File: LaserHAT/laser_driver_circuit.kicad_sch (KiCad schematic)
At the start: 24 parts, among them Q1 Si2302CDS, Q2 Si1902DL, U1 TLV2371DBV

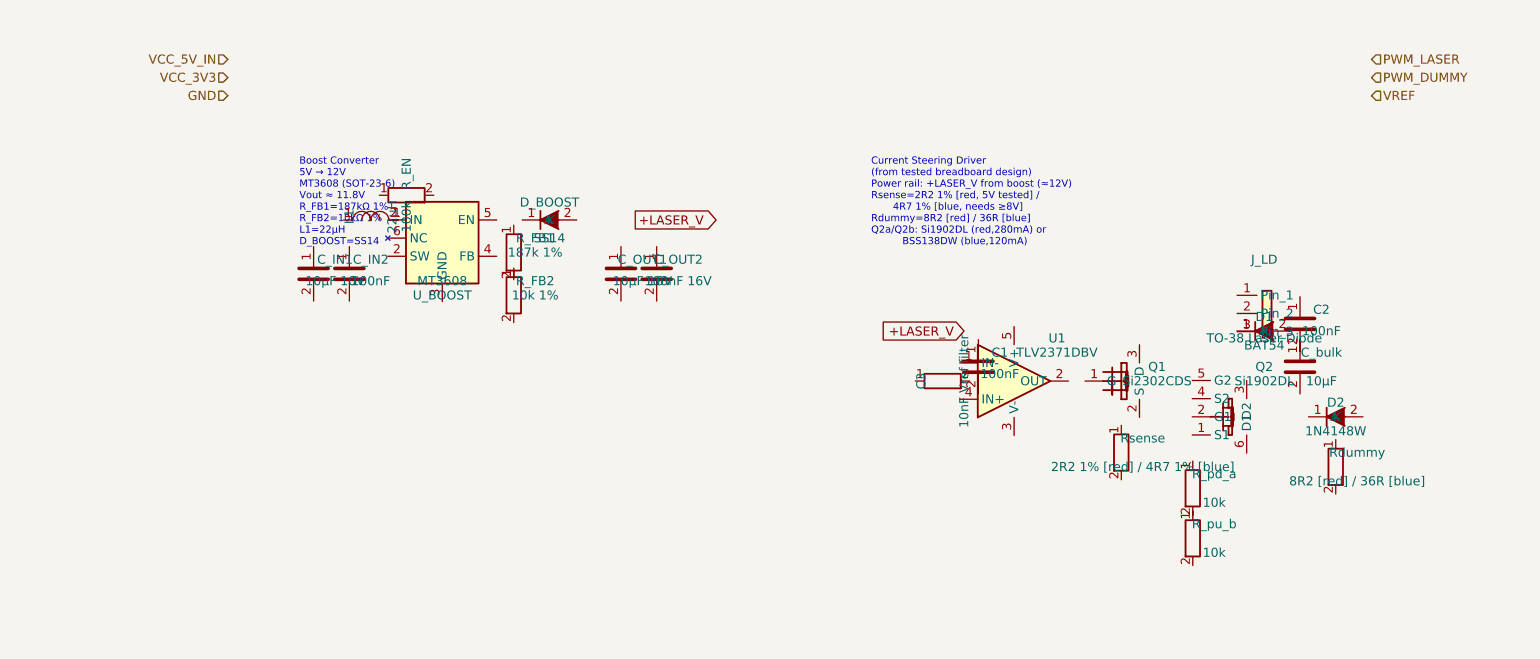
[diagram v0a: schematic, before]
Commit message: Regenerate schematics via kiutils; add generate_schematics.py
Previous hand-written schematics failed to open in eeschema due to
quoted UUIDs and unrecognised generator_version field.  Replace with
a kiutils-based Python generator that produces correctly-formatted
KiCad 9 S-expressions.

Each sheet now has:
- Unquoted UUIDs and proper PageSettings object (eeschema-compatible)
- HierarchicalLabel port declarations matching parent sheet pins
- LocalLabel net labels placed at exact pin connection points so KiCad
  can build the netlist without manual wire routing
- NoConnect markers on unused pins (SBU1/SBU2, DTR, MT3608 NC pin)
- SymbolInstance entries for BOM/netlist annotation

Add requirements.txt (kiutils==1.4.8) for reproducible environment.

Run: .venv/bin/python3 LaserHAT/generate_schematics.py

Co-Authored-By: Claude Sonnet 4.6 <noreply@anthropic.com>
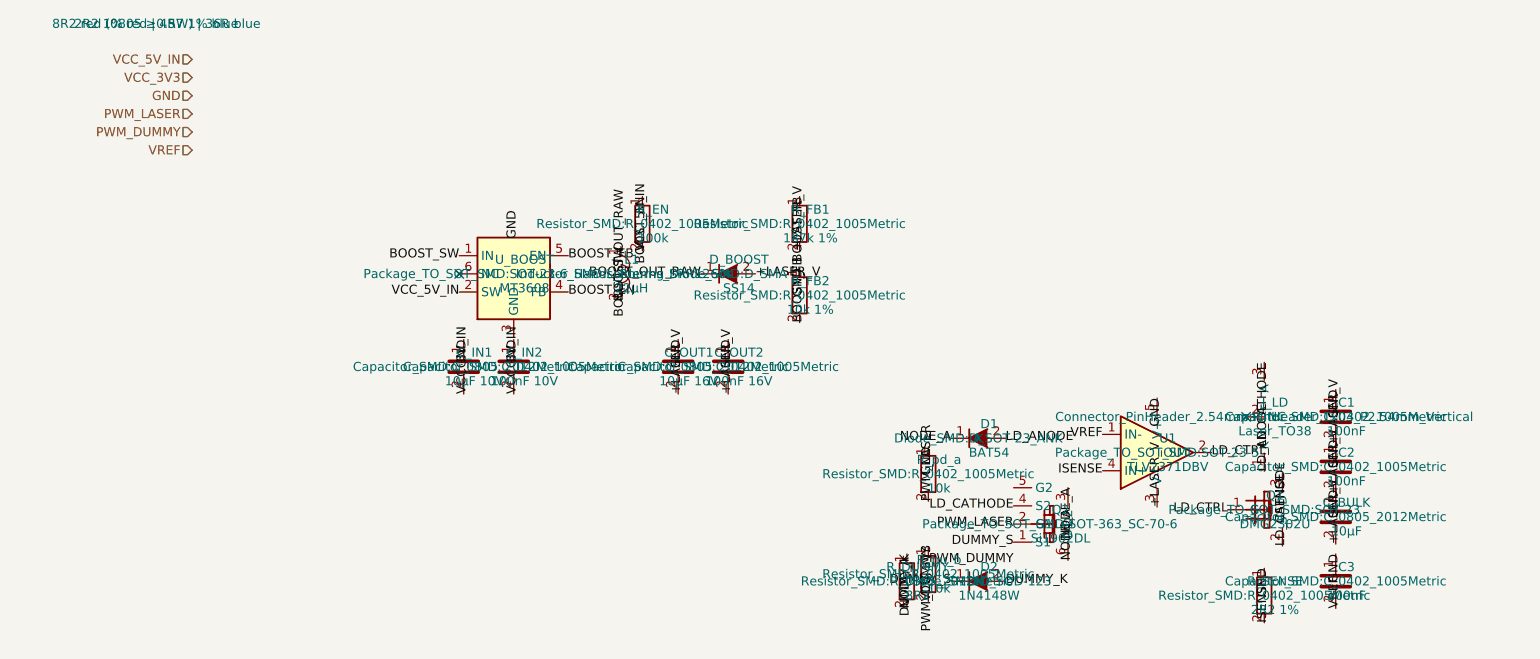
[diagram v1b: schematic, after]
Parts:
- removed C3: 10nF Vref filter, Capacitor_SMD:C_0402_1005Metric, symbol Device:R
- removed C_bulk: 10µF, Capacitor_SMD:C_0805_2012Metric, symbol Device:C
- removed J_LD: TO-38 Laser Diode, Connector_PinHeader_2.54mm:PinHeader_1x03_P2.54mm_Vertical, symbol Connector_Generic:Conn_01x03
- removed Rdummy: 8R2 [red] / 36R [blue], Resistor_SMD:R_0805_2012Metric, symbol Device:R
- removed Rsense: 2R2 1% [red] / 4R7 1% [blue], Resistor_SMD:R_0402_1005Metric, symbol Device:R
- added C3: 100nF, Capacitor_SMD:C_0402_1005Metric, symbol Device:C
- added C_BULK: 10µF, Capacitor_SMD:C_0805_2012Metric, symbol Device:C
- added J_LD: Laser_TO38, Connector_PinHeader_2.54mm:PinHeader_1x03_P2.54mm_Vertical, symbol Device:D_Laser_Photo_NType
- added R_DUMMY: 8R2, Resistor_SMD:R_0805_2012Metric, symbol Device:R
- added R_SENSE: 2R2 1%, Resistor_SMD:R_0402_1005Metric, symbol Device:R
- C_IN2: value 100nF -> 100nF 10V
- D1: footprint Diode_SMD:D_SOT-23_AnodeK1K2 -> Diode_SMD:D_SOT-23_ANK
- L1: footprint Inductor_SMD:L_4020 -> Inductor_SMD:L_Bourns_SRR1260
- Q1: value Si2302CDS -> DMG2302U
- U_BOOST: footprint Package_TO_SOT_SMD:SOT-23-6 -> Package_TO_SOT_SMD:SOT-23-6_Handsoldering
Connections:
- net +LASER_V: now also C1.2, C2.2, C_OUT1.2, C_OUT2.2, D_BOOST.2 (K), R_FB1.2, U1.3 (V-), C_BULK.2
- net GND: now also C1.1, C2.1, C_IN1.1, C_IN2.1, C_OUT1.1, C_OUT2.1, R_FB2.1, R_pd_a.1, U1.5 (V+), C3.1, C_BULK.1, R_SENSE.1
- net PWM_DUMMY: now also R_pu_b.1
- net PWM_LASER: now also Q2.2 (G1), R_pd_a.2
- net VCC_3V3: now also R_pu_b.2
- net VCC_5V_IN: now also C_IN1.2, C_IN2.2, R_EN.2, U_BOOST.2 (SW)
- net VREF: now also U1.1 (IN-), C3.2
- net BOOST_SW: now reaches U_BOOST.1 (IN)
- net BOOST_SW: now also L1.1
- net BOOST_EN: now reaches U_BOOST.4 (FB)
- net BOOST_EN: now also R_EN.1
- net BOOST_FB: now reaches U_BOOST.5 (EN)
- net BOOST_FB: now also R_FB1.1, R_FB2.2
- net BOOST_OUT_RAW: now reaches L1.2
- net BOOST_OUT_RAW: now also D_BOOST.1 (A)
- net LD_CTRL: now reaches U1.2 (OUT)
- net LD_CTRL: now also Q1.1 (G)
- net ISENSE: now reaches U1.4 (IN+)
- net ISENSE: now also Q1.3 (D), R_SENSE.2
- net LD_CATHODE: now reaches Q1.2 (S)
- net LD_CATHODE: now also Q2.4 (S2), J_LD.3 (A)
- net DUMMY_S: now reaches Q2.1 (S1)
- net DUMMY_S: now also D2.1 (A)
- net NODE_A: now reaches Q2.3 (D2)
- net NODE_A: now also D1.1 (A), Q2.6 (D1), R_DUMMY.2
- net LD_ANODE: now reaches D1.2 (K)
- net LD_ANODE: now also J_LD.1 (K)
- net DUMMY_K: now reaches D2.2 (K)
- net DUMMY_K: now also R_DUMMY.1
- no-connect marks 0 -> 2
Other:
- note removed: "Boost Converter 5V → 12V MT3608 (SOT-23-6) Vout ≈ 11.8V R_FB1=187kΩ 1% R_FB2=10kΩ 1% L1=22µH D_BOOST=SS14"
- note removed: "Current Steering Driver (from tested breadboard design) Power rail: +LASER_V from boost (≈12V) Rsense=2R2 1% [red, 5V tested] / 4R7 1% [blue, needs ≥8V] Rdummy=8R2 [red] / 36R [blue] Q2a/Q2b: Si1902DL (red,280mA) or BSS138DW (blue,120mA)"
- title: Laser Driver Circuit — Boost + Current Steering -> Laser Driver Circuit

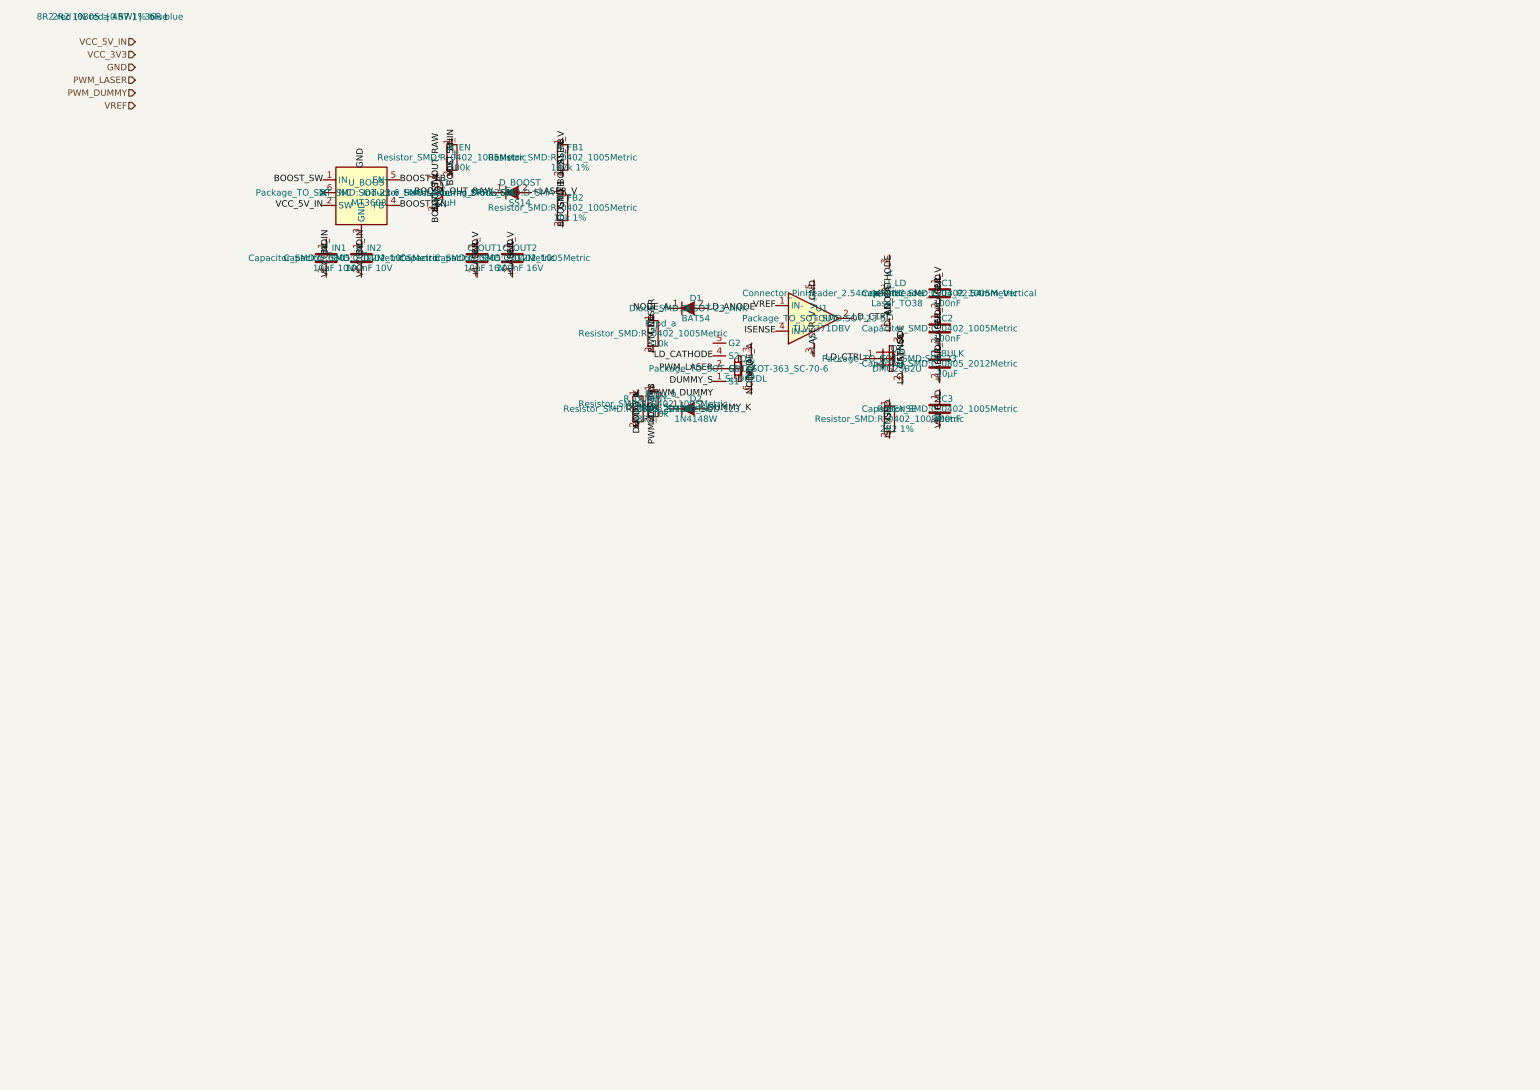
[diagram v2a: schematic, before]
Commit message: Implement schematic design rules; add CLAUDE.md
- Rule 1: hide pin names/numbers on passive parts (R, C, L)
- Rule 2: add ≥5mm wire stub before every net label
- Rule 3: preserve hand-edited laser_driver.kicad_sch by loading from PCB/ original
- Rule 4: generous component spacing across multiple sheets
- Add CLAUDE.md documenting all rules, setup, signal naming, and kiutils conventions

Co-Authored-By: Claude Sonnet 4.6 <noreply@anthropic.com>
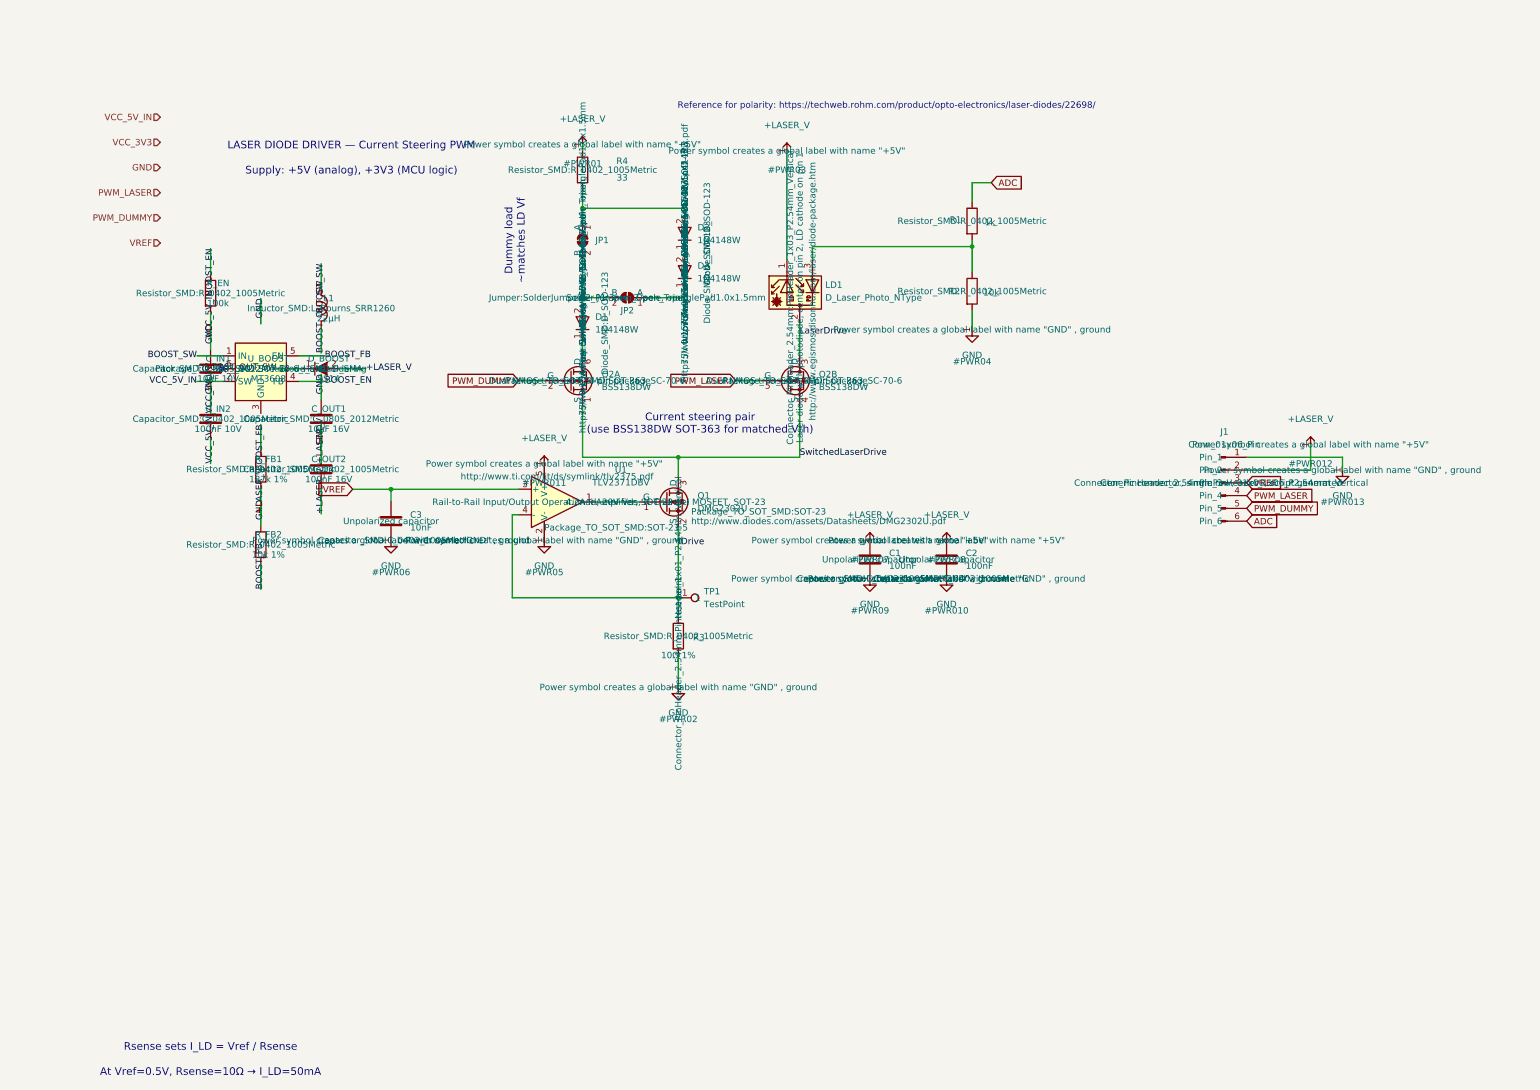
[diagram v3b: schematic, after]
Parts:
- removed C_BULK: 10µF, Capacitor_SMD:C_0805_2012Metric, symbol Device:C
- removed D1: BAT54, Diode_SMD:D_SOT-23_ANK, symbol Diode:BAT54
- removed J_LD: Laser_TO38, Connector_PinHeader_2.54mm:PinHeader_1x03_P2.54mm_Vertical, symbol Device:D_Laser_Photo_NType
- removed R_DUMMY: 8R2, Resistor_SMD:R_0805_2012Metric, symbol Device:R
- removed R_SENSE: 2R2 1%, Resistor_SMD:R_0402_1005Metric, symbol Device:R
- removed R_pd_a, R_pu_b: 10k, Resistor_SMD:R_0402_1005Metric, symbol Device:R
- added D1, D3: 1N4148W, Diode_SMD:D_SOD-123, symbol Diode:1N4148W
- added J1: Conn_01x06_Pin, Connector_PinHeader_2.54mm:PinHeader_1x06_P2.54mm_Vertical, symbol Connector:Conn_01x06_Pin
- added JP1, JP2: ~, Jumper:SolderJumper-2_P1.3mm_Open_TrianglePad1.0x1.5mm, symbol Jumper:SolderJumper_2_Open
- added LD1: D_Laser_Photo_NType, Connector_PinHeader_2.54mm:PinHeader_1x03_P2.54mm_Vertical, symbol Device:D_Laser_Photo_NType
- added unit 2 of Q2
- added R1: 1k, Resistor_SMD:R_0402_1005Metric, symbol Device:R
- added R2: 10k, Resistor_SMD:R_0402_1005Metric, symbol Device:R
- added R3: 10Ω 1%, Resistor_SMD:R_0402_1005Metric, symbol Device:R
- added R4: 33, Resistor_SMD:R_0402_1005Metric, symbol Device:R
- added TP1: TestPoint, Connector_PinHeader_2.54mm:PinHeader_1x01_P2.54mm_Vertical, symbol Connector:TestPoint
- C3: value 100nF -> 10nF
- Q2: value Si1902DL -> BSS138DW
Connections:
- net VCC_5V_IN is gone; now on net +LASER_V: C_IN1.2, C_IN2.2, R_EN.2, U_BOOST.2 (SW)
- net +LASER_V: now also C1.1, C2.1, C3.2, C_IN1.1, C_IN2.1, C_OUT1.1, C_OUT2.1, R_FB2.1, U1.2 (V-), U1.5 (V+), J1.1 (Pin_1), J1.2 (Pin_2), LD1.1, R2.2, R3.2, R4.1; no longer U1.3 (V-)
- net PWM_DUMMY: now also Q2.2 (G), J1.5 (Pin_5)
- net PWM_LASER: now also J1.4 (Pin_4), Q2.5 (G); no longer Q2.2 (G1)
- net VREF: now also C3.1, U1.3 (+), J1.3 (Pin_3); no longer C3.2, U1.1 (IN-)
- net BOOST_OUT_RAW renamed BOOST_OUT_SW
- net DUMMY_K: no longer names the net of D2.2 (A)
- net DUMMY_K: now also JP1.1 (A), R4.2
- net DUMMY_S: no longer names the net of D2.1 (K)
- net DUMMY_S: now also D3.2 (A); no longer Q2.1 (S1)
- removed net GND: C1.1, C2.1, C3.1, C_IN1.1, C_IN2.1, C_OUT1.1, C_OUT2.1, R_FB2.1, U1.5 (V+)
- net ISENSE renamed IDrive
- net IDrive: now also Q1.2 (S), R3.1, TP1.1; no longer Q1.3 (D)
- removed net LD_CATHODE: Q1.2 (S), Q2.4 (S2)
- net LD_CTRL: no longer names the net of Q1.1 (G)
- net LD_CTRL: now also U1.1; no longer U1.2 (OUT)
- net NODE_A: no longer names the net of Q2.6 (D)
- net NODE_A: now also D1.1 (K); no longer Q2.3 (D2)
- new net: D3.1 (K), JP2.1 (A)
- new net: LD1.3, R1.2, R2.1
- new net: D1.2 (A), JP1.2 (B), JP2.2 (B)
- new net ADC: J1.6 (Pin_6), R1.1
- new net LaserDrive: LD1.2, Q2.3 (D)
- new net SwitchedLaserDrive: Q1.3 (D), Q2.1 (S), Q2.4 (S)
- no-connect marks 2 -> 1
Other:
- note added: "At Vref=0.5V, Rsense=10Ω → I_LD=50mA"
- note added: "Current steering pair (use BSS138DW SOT-363 for matched Vth)"
- note added: "Dummy load ~matches LD Vf"
- note added: "LASER DIODE DRIVER — Current Steering PWM"
- note added: "Reference for polarity: https://techweb.rohm.com/product/opto-electronics/laser-diodes/22698/"
- note added: "Rsense sets I_LD = Vref / Rsense"
- note added: "Supply: +5V (analog), +3V3 (MCU logic)"

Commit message: Fix three schematic generation bugs
- Symbol unit names: set entryName on manually-created Symbol units so
  they serialize as "+LASER_V_0_1" not "None_0_1" (KiCad load error)
- Passive pin hiding: set pinNames=True alongside pinNamesHide=True so
  the (pin_names hide) token is actually emitted for Device:C and Device:L
- Property visibility: hide Footprint/Datasheet/Description on all
  schematic symbol instances; only Reference and Value remain shown

Co-Authored-By: Claude Sonnet 4.6 <noreply@anthropic.com>
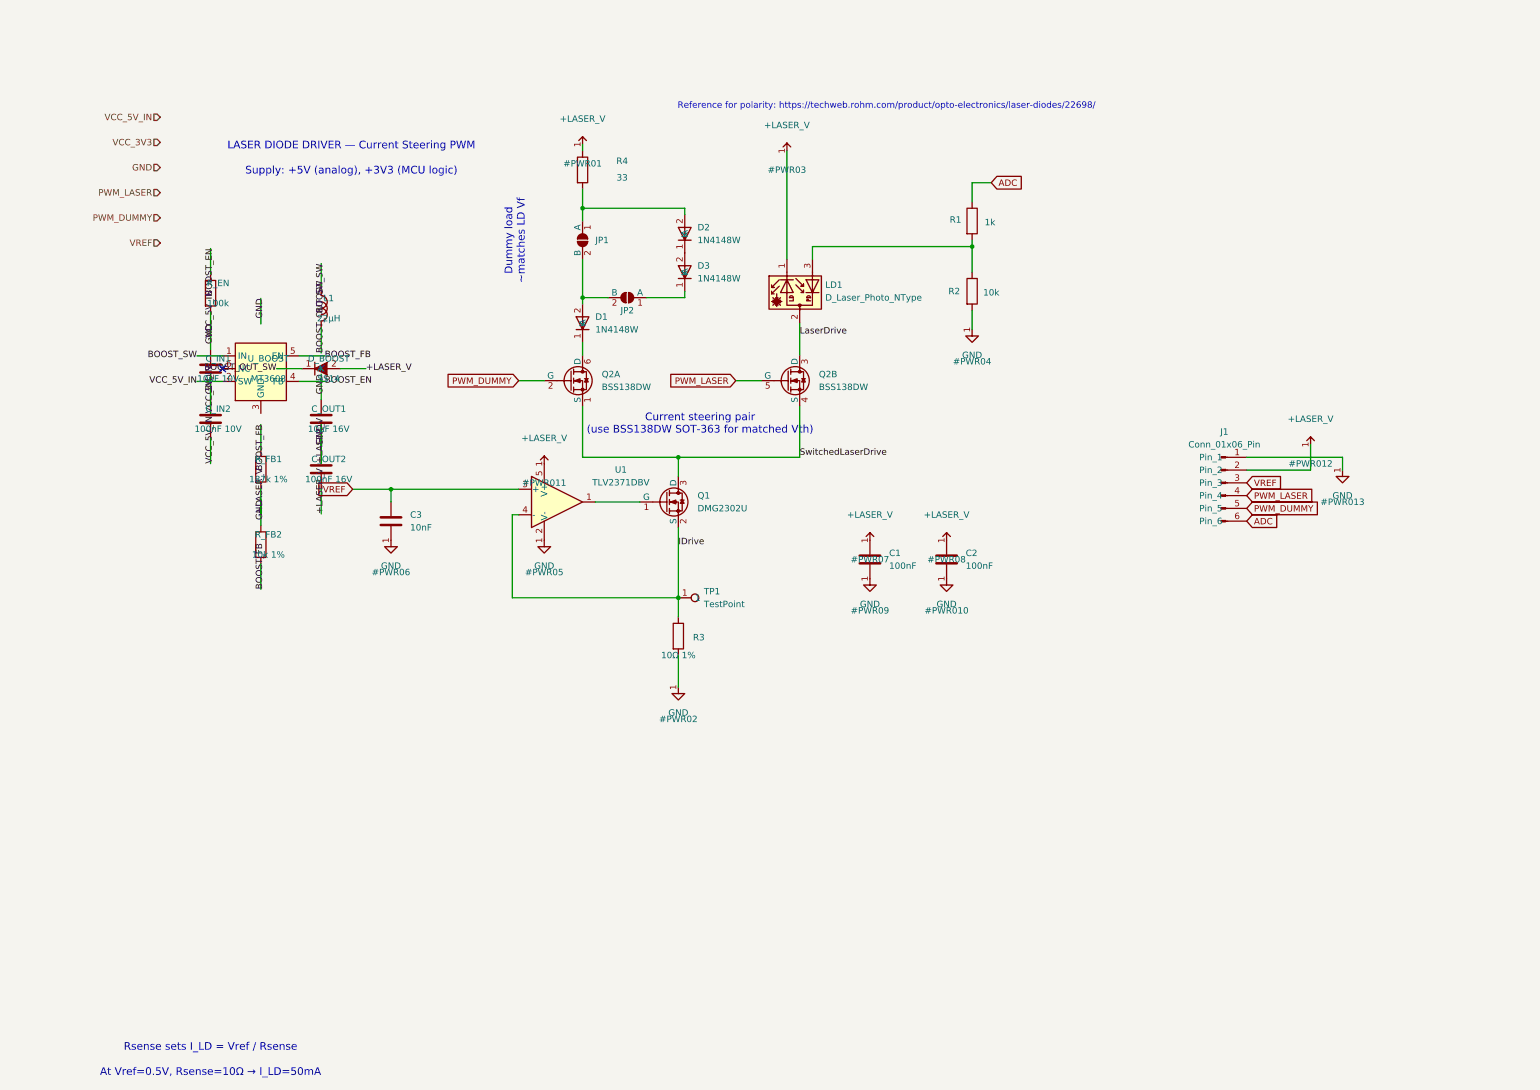
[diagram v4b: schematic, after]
